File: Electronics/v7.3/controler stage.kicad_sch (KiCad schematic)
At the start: 25 parts, among them IC4 RTC PCF8523T, J1 Conn_06Pins, SW2 SPST_TACT-KMR2, U1 ATSAMD21G18A, U4 Adafruit LCD Screen, X1 ClockXtal, X2 uXtal, X4 microsd

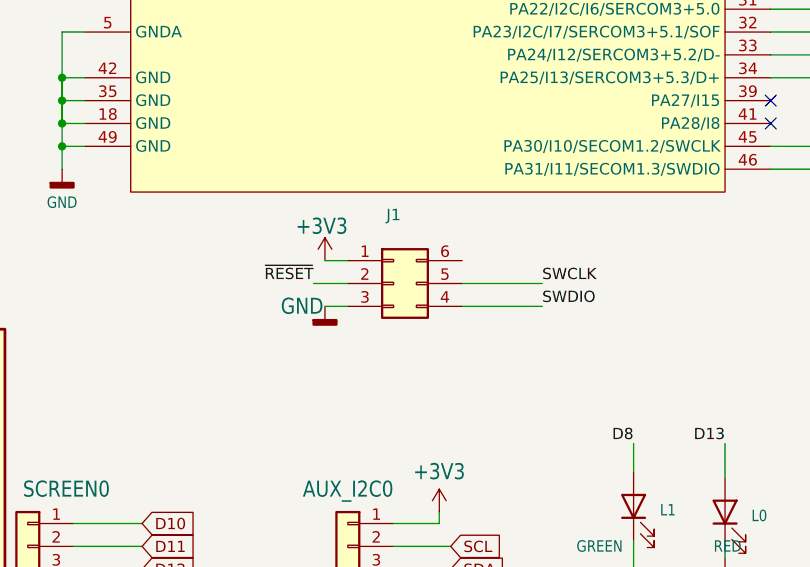
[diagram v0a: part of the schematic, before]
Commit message: Fixd some MPN and regenerated the BOM.
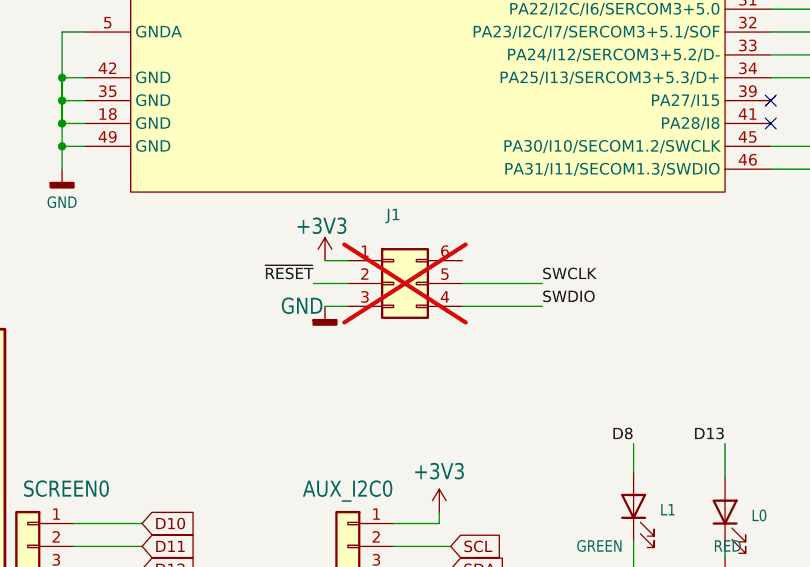
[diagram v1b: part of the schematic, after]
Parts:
- J1: now not fitted; now left out of the parts list
- L1: MPN 150060VS75000 -> LTST-C191KGKT
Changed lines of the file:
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@@
 			)
 		)
-		(property "MPN" "150060VS75000"
+		(property "MPN" "LTST-C191KGKT"
 			(at 105.41 160.655 0)
 			(effects
@@
 		(unit 1)
 		(exclude_from_sim no)
-		(in_bom yes)
-		(on_board yes)
-		(dnp no)
+		(in_bom no)
+		(on_board yes)
+		(dnp yes)
 		(property "Reference" "J1"
 			(at 78.74 128.27 0)

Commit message: Replaced RED LED because it's obsolete.
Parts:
- L0: MPN 5975004407F -> VFHR1116P-4C82A-TR; OEPSPN OEPS030006 -> OEPS030038
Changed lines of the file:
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@@
 			)
 		)
-		(property "OEPSPN" "OEPS030006"
+		(property "OEPSPN" "OEPS030038"
 			(at 115.57 161.29 0)
 			(effects
@@
 			)
 		)
-		(property "MPN" "5975004407F"
+		(property "MPN" "VFHR1116P-4C82A-TR"
 			(at 115.57 161.29 0)
 			(effects
